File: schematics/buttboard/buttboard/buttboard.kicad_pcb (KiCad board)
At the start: 4 copper layers, 84 x 65 mm, 11 parts, among them J1 Conn_01x05

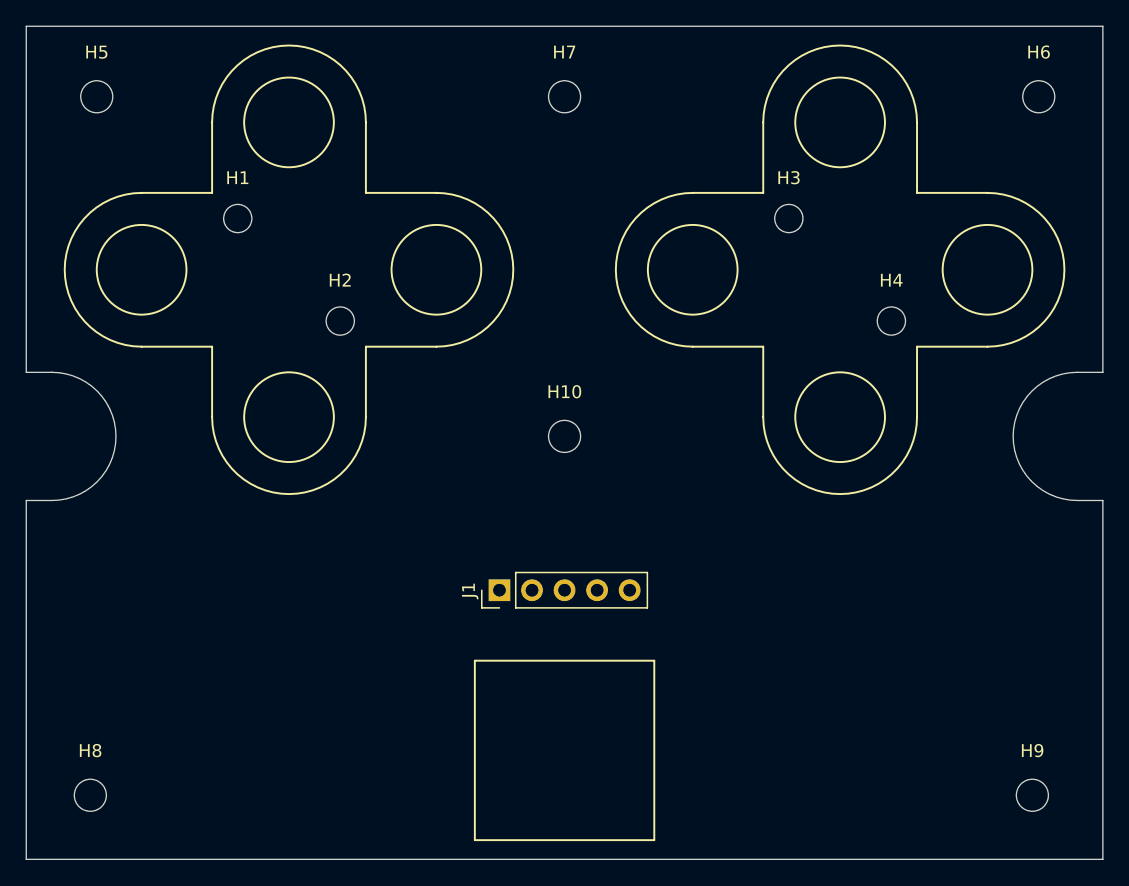
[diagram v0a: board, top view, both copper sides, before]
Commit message: Mounting points for mainboard added. Adjusted position of track ball on buttboard.
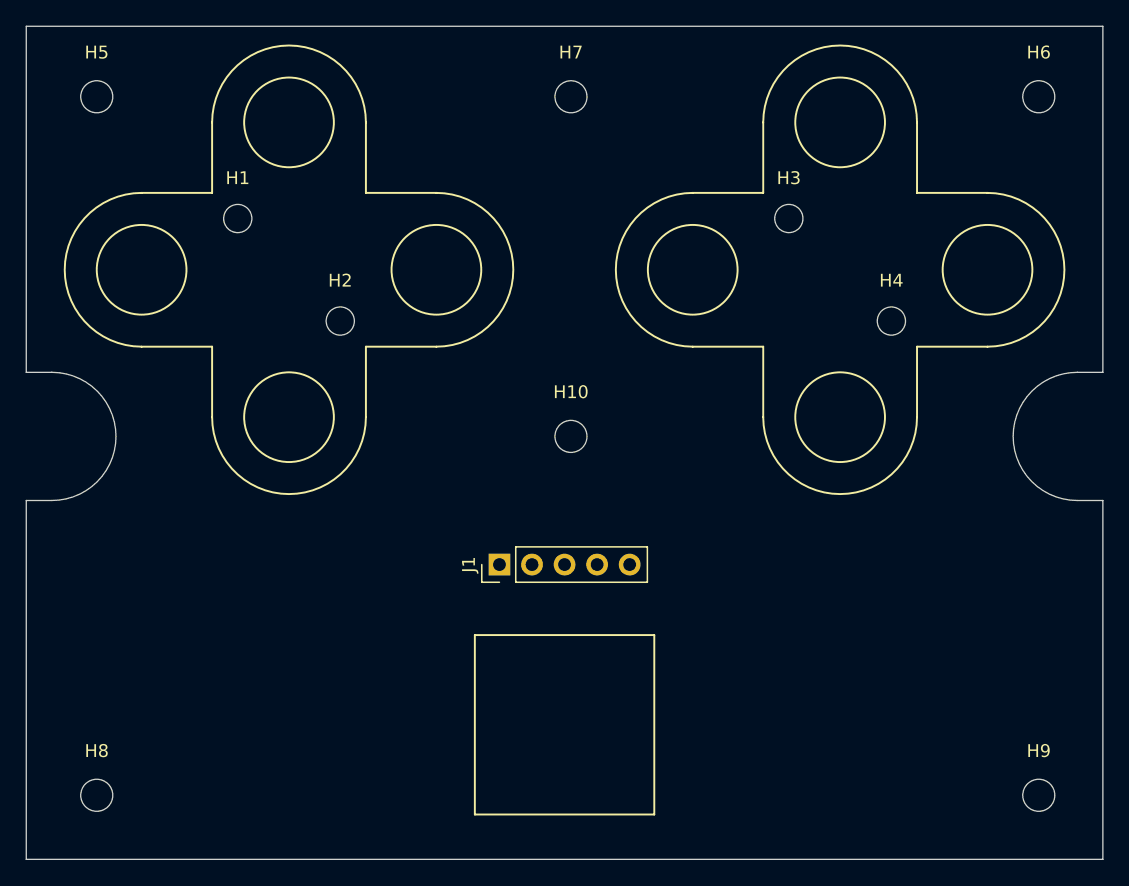
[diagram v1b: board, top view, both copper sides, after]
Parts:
- moved J1 2.00 mm to (147.4, 99.0)
- moved H10 0.50 mm to (153.0, 89.0)
- moved H7 0.50 mm to (153.0, 62.5)
- moved H8 0.50 mm to (116.0, 117.0)
- moved H9 0.50 mm to (189.5, 117.0)
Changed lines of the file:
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@@
 	(footprint "Connector_PinHeader_2.54mm:PinHeader_1x05_P2.54mm_Vertical"
 		(layer "F.Cu")
-		(at 147.42 101 90)
+		(at 147.42 99 90)
 		(descr "Through hole straight pin header, 1x05, 2.54mm pitch, single row")
 		(tags "Through hole pin header THT 1x05 2.54mm single row")
@@
 	(footprint "MountingHole:MountingHole_2.5mm"
 		(layer "F.Cu")
-		(at 115.5 117)
+		(at 116 117)
 		(descr "Mounting Hole 2.5mm, no annular, generated by kicad-footprint-generator mountinghole.py")
 		(tags "mountinghole")
@@
 	(footprint "MountingHole:MountingHole_2.5mm"
 		(layer "F.Cu")
-		(at 189 117)
+		(at 189.5 117)
 		(descr "Mounting Hole 2.5mm, no annular, generated by kicad-footprint-generator mountinghole.py")
 		(tags "mountinghole")
@@
 	(footprint "MountingHole:MountingHole_2.5mm"
 		(layer "F.Cu")
-		(at 152.5 62.5)
+		(at 153 62.5)
 		(descr "Mounting Hole 2.5mm, no annular, generated by kicad-footprint-generator mountinghole.py")
 		(tags "mountinghole")
@@
 	(footprint "MountingHole:MountingHole_2.5mm"
 		(layer "F.Cu")
-		(at 152.5 89)
+		(at 153 89)
 		(descr "Mounting Hole 2.5mm, no annular, generated by kicad-footprint-generator mountinghole.py")
 		(tags "mountinghole")
@@
 	)
 	(gr_rect
-		(start 145.5 106.5)
-		(end 159.5 120.5)
+		(start 145.5 104.5)
+		(end 159.5 118.5)
 		(stroke
 			(width 0.15)
@@
 	)
 	(gr_line
-		(start 152.5 129.5)
-		(end 152.5 46.5)
+		(start 153 129.5)
+		(end 153 46.5)
 		(stroke
 			(width 0.15)
@@
 		(layer "F.SilkS")
 		(pts
-			(xy 116 62.5) (xy 152.5 62.5)
+			(xy 116 117) (xy 110.5 118.5)
+		)
+		(height 8)
+		(orientation 0)
+		(format
+			(prefix "")
+			(suffix "")
+			(units 3)
+			(units_format 0)
+			(precision 4)
+			(suppress_zeroes yes)
+		)
+		(style
+			(thickness 0.15)
+			(arrow_length 1.27)
+			(text_position_mode 0)
+			(arrow_direction outward)
+			(extension_height 0.58642)
+			(extension_offset 0.5)
+			(keep_text_aligned yes)
+		)
+		(gr_text "5,5"
+			(at 113.25 123.85 0)
+			(layer "F.SilkS")
+			(effects
+				(font
+					(size 1 1)
+					(thickness 0.15)
+				)
+			)
+		)
+	)
+	(dimension
+		(type orthogonal)
+		(layer "F.SilkS")
+		(pts
+			(xy 159.5 111.5) (xy 194.5 111.5)
+		)
+		(height -2)
+		(orientation 0)
+		(format
+			(prefix "")
+			(suffix "")
+			(units 3)
+			(units_format 0)
+			(precision 4)
+			(suppress_zeroes yes)
+		)
+		(style
+			(thickness 0.15)
+			(arrow_length 1.27)
+			(text_position_mode 0)
+			(arrow_direction outward)
+			(extension_height 0.58642)
+			(extension_offset 0.5)
+			(keep_text_aligned yes)
+		)
+		(gr_text "35"
+			(at 177 108.35 0)
+			(layer "F.SilkS")
+			(effects
+				(font
+					(size 1 1)
+					(thickness 0.15)
+				)
+			)
+		)
+	)
+	(dimension
+		(type orthogonal)
+		(layer "F.SilkS")
+		(pts
+			(xy 116 62.5) (xy 110.5 61.5)
+		)
+		(height -8.5)
+		(orientation 0)
+		(format
+			(prefix "")
+			(suffix "")
+			(units 3)
+			(units_format 0)
+			(precision 4)
+			(suppress_zeroes yes)
+		)
+		(style
+			(thickness 0.15)
+			(arrow_length 1.27)
+			(text_position_mode 0)
+			(arrow_direction outward)
+			(extension_height 0.58642)
+			(extension_offset 0.5)
+			(keep_text_aligned yes)
+		)
+		(gr_text "5,5"
+			(at 113.25 52.85 0)
+			(layer "F.SilkS")
+			(effects
+				(font
+					(size 1 1)
+					(thickness 0.15)
+				)
+			)
+		)
+	)
+	(dimension
+		(type orthogonal)
+		(layer "F.SilkS")
+		(pts
+			(xy 116.5 62.5) (xy 153 62.5)
 		)
 		(height -21)
@@
 		)
 		(gr_text "36,5"
-			(at 134.25 40.35 0)
+			(at 134.75 40.35 0)
 			(layer "F.SilkS")
 			(effects
@@
 		(layer "F.SilkS")
 		(pts
+			(xy 145.5 108) (xy 110.5 107.5)
+		)
+		(height 2.5)
+		(orientation 0)
+		(format
+			(prefix "")
+			(suffix "")
+			(units 3)
+			(units_format 0)
+			(precision 4)
+			(suppress_zeroes yes)
+		)
+		(style
+			(thickness 0.15)
+			(arrow_length 1.27)
+			(text_position_mode 0)
+			(arrow_direction outward)
+			(extension_height 0.58642)
+			(extension_offset 0.5)
+			(keep_text_aligned yes)
+		)
+		(gr_text "35"
+			(at 128 109.35 0)
+			(layer "F.SilkS")
+			(effects
+				(font
+					(size 1 1)
+					(thickness 0.15)
+				)
+			)
+		)
+	)
+	(dimension
+		(type orthogonal)
+		(layer "F.SilkS")
+		(pts
 			(xy 116 62.5) (xy 115.5 117)
 		)
@@
 		(layer "F.SilkS")
 		(pts
-			(xy 152.5 62.5) (xy 189.5 62.5)
+			(xy 153 62.5) (xy 189.5 62.5)
 		)
 		(height -21)
@@
 			(keep_text_aligned yes)
 		)
-		(gr_text "37"
-			(at 171 40.35 0)
+		(gr_text "36,5"
+			(at 171.25 40.35 0)
 			(layer "F.SilkS")
 			(effects
@@
 		(layer "F.SilkS")
 		(pts
-			(xy 115.5 117) (xy 189 117)
+			(xy 116 117) (xy 189.5 117)
 		)
 		(height 9.5)
@@
 		)
 		(gr_text "73,5"
-			(at 152.25 125.35 0)
+			(at 152.75 125.35 0)
 			(layer "F.SilkS")
 			(effects
@@
 			(effects
 				(font
-					(size 1 1)
-					(thickness 0.15)
-				)
-			)
-		)
-	)
-	(dimension
-		(type orthogonal)
-		(layer "Edge.Cuts")
-		(pts
-			(xy 152.5 94) (xy 117.5 94)
-		)
-		(height 18)
-		(orientation 0)
-		(format
-			(prefix "")
-			(suffix "")
-			(units 3)
-			(units_format 0)
-			(precision 4)
-			(suppress_zeroes yes)
-		)
-		(style
-			(thickness 0.1)
-			(arrow_length 1.27)
-			(text_position_mode 0)
-			(arrow_direction outward)
-			(extension_height 0.58642)
-			(extension_offset 0.5)
-			(keep_text_aligned yes)
-		)
-		(gr_text "35"
-			(at 135 110.85 0)
-			(layer "Edge.Cuts")
-			(effects
-				(font
-					(size 1 1)
-					(thickness 0.15)
-				)
-			)
-		)
-	)
-	(dimension
-		(type orthogonal)
-		(layer "Edge.Cuts")
-		(pts
-			(xy 152.5 94) (xy 187.5 94)
-		)
-		(height 17)
-		(orientation 0)
-		(format
-			(prefix "")
-			(suffix "")
-			(units 3)
-			(units_format 0)
-			(precision 4)
-			(suppress_zeroes yes)
-		)
-		(style
-			(thickness 0.1)
-			(arrow_length 1.27)
-			(text_position_mode 0)
-			(arrow_direction outward)
-			(extension_height 0.58642)
-			(extension_offset 0.5)
-			(keep_text_aligned yes)
-		)
-		(gr_text "35"
-			(at 170 109.85 0)
-			(layer "Edge.Cuts")
-			(effects
-				(font

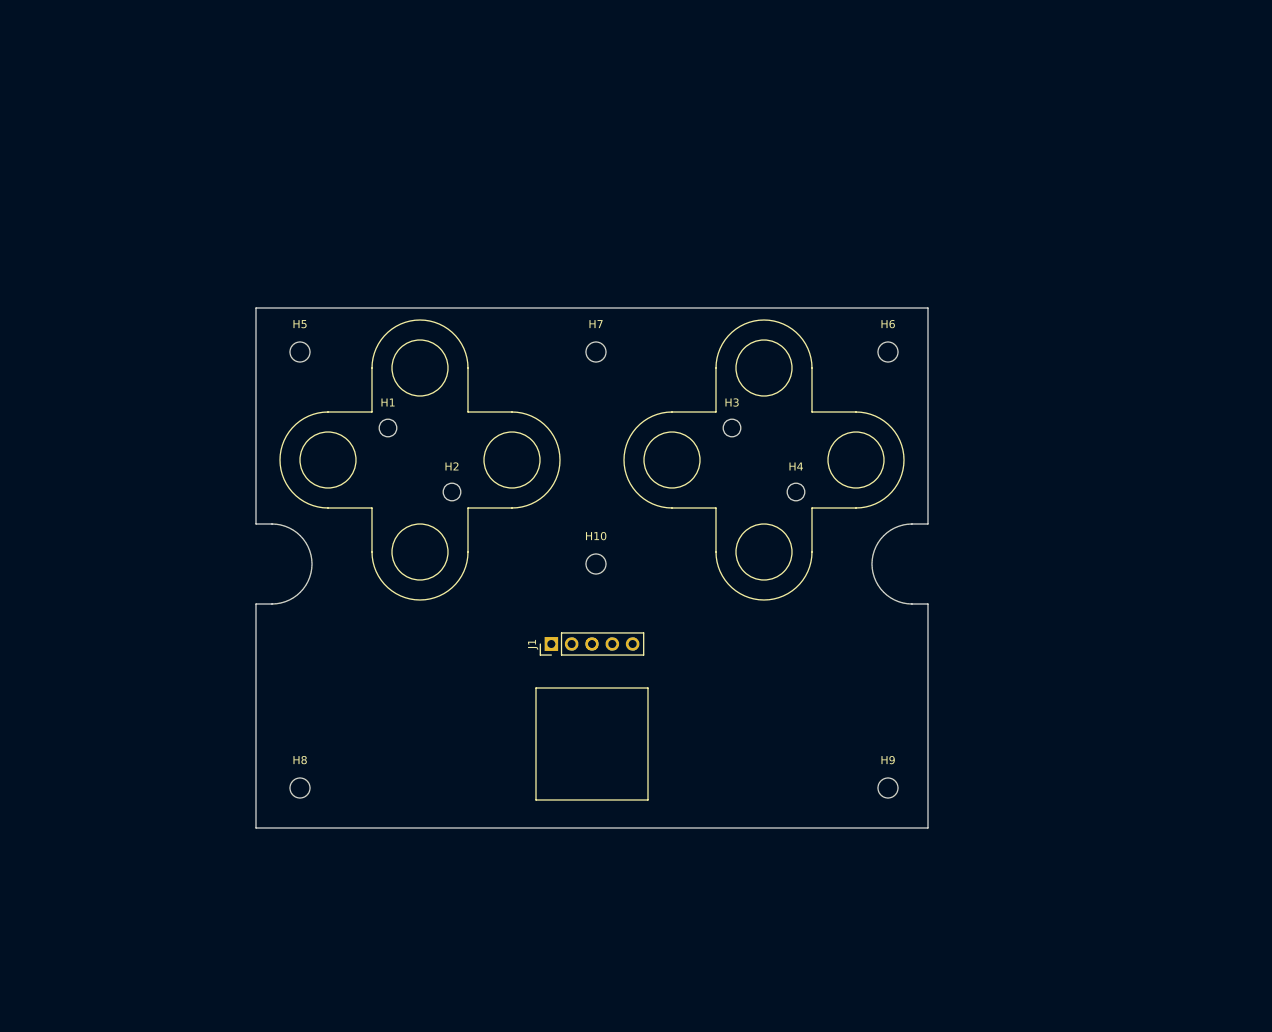
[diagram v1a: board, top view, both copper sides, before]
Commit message: Added membrane button footprint to buttboard.
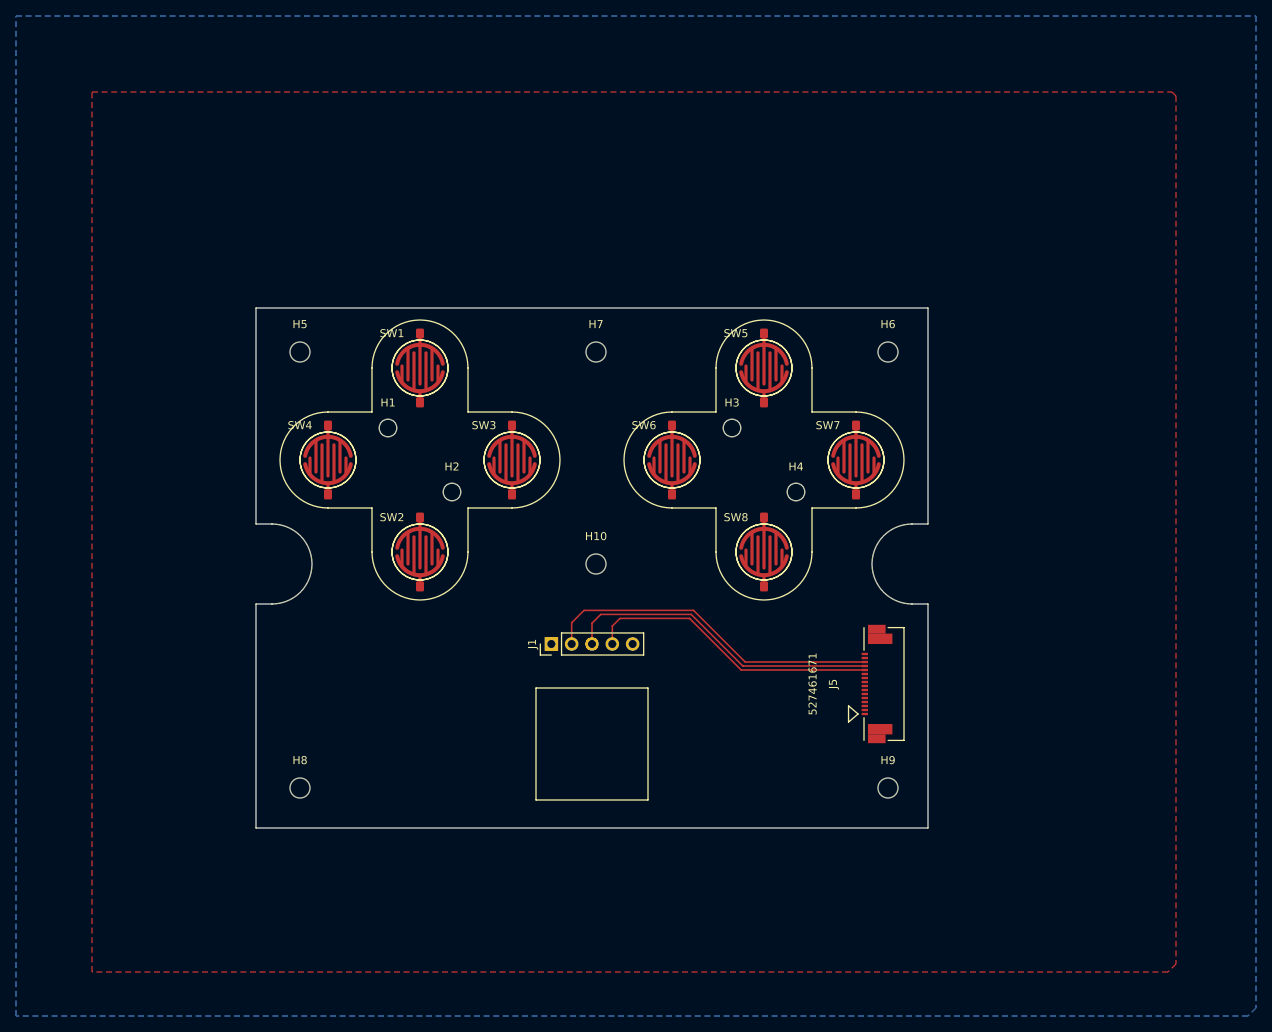
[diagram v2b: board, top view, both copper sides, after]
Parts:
- added J5: 527461671, CON_527461671_MOL:CON_527461671_MOL, F.Cu at (189.0, 104.0)
- added SW1: N, MEMBRANE:MEMBRANE_A, F.Cu at (131.0, 64.5)
- added SW2: S, MEMBRANE:MEMBRANE_A, F.Cu at (131.0, 87.5)
- added SW3: E, MEMBRANE:MEMBRANE_A, F.Cu at (142.5, 76.0)
- added SW4: W, MEMBRANE:MEMBRANE_A, F.Cu at (119.5, 76.0)
- added SW5: A, MEMBRANE:MEMBRANE_A, F.Cu at (174.0, 64.5)
- added SW6: B, MEMBRANE:MEMBRANE_A, F.Cu at (162.5, 76.0)
- added SW7: C, MEMBRANE:MEMBRANE_A, F.Cu at (185.5, 76.0)
- added SW8: D, MEMBRANE:MEMBRANE_A, F.Cu at (174.0, 87.5)
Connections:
- J1 pad 2: TB_INT -> TRACKBALL_INTERRUPT
- J1 pad 3: TB_SCL -> I2C_SCL
- J1 pad 4: TB_SDA -> I2C_SDA
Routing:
- net TRACKBALL_INTERRUPT: track 0.00 -> 42.6 mm
- net I2C_SCL: track 0.00 -> 39.8 mm
- net I2C_SDA: track 0.00 -> 36.9 mm
- added copper zone on B.Cu, net GND
- added copper zone on F.Cu, net GND
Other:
- copper layers 4 -> 2

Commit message: Replaced membrane buttons with tactile buttons on buttboard.
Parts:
- SW1, SW2, SW3, SW4, SW5, SW6, SW7, SW8: footprint MEMBRANE:MEMBRANE_A -> Button_Switch_THT:SW_PUSH_6mm_H7.3mm
- moved SW1 3.95 mm to (127.8, 62.2)
- moved SW2 3.95 mm to (127.8, 85.2)
- moved SW3 3.95 mm to (139.2, 73.8)
- moved SW4 3.95 mm to (116.2, 73.8)
- moved SW5 3.95 mm to (170.8, 62.2)
- moved SW6 3.95 mm to (159.2, 73.8)
- moved SW7 3.95 mm to (182.2, 73.8)
- moved SW8 3.95 mm to (170.8, 85.2)
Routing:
- net BTN_A: track 0.00 -> 56.0 mm, vias 0 -> 1
- net BTN_B: track 0.00 -> 47.4 mm, vias 0 -> 1
- net BTN_C: track 0.00 -> 44.7 mm, vias 0 -> 1
- net BTN_D: track 0.00 -> 30.4 mm, vias 0 -> 1
- net 3V3: track 0.00 -> 29.7 mm, vias 0 -> 1

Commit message: More work on buttboard.
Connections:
- J5 pad 6: unconnected-(J5-Pad6) -> BTN_DPAD_N
- J5 pad 7: unconnected-(J5-Pad7) -> BTN_DPAD_S
- J5 pad 8: unconnected-(J5-Pad8) -> BTN_DPAD_E
- J5 pad 9: unconnected-(J5-Pad9) -> BTN_DPAD_W
- SW1 pad 1: unconnected-(SW1-Pad1) -> BTN_DPAD_N
- SW2 pad 1: unconnected-(SW2-Pad1) -> BTN_DPAD_S
- SW3 pad 1: unconnected-(SW3-Pad1) -> BTN_DPAD_E
- SW4 pad 1: unconnected-(SW4-Pad1) -> BTN_DPAD_W
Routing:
- net BTN_DPAD_N: track 0.00 -> 118.5 mm, vias 0 -> 1
- net BTN_DPAD_W: track 0.00 -> 101.2 mm
- net BTN_DPAD_E: track 0.00 -> 86.2 mm, vias 0 -> 1
- net BTN_DPAD_S: track 0.00 -> 84.2 mm, vias 0 -> 1
- net BTN_A: track 56.0 -> 64.8 mm
- net BTN_D: track 30.4 -> 39.1 mm
- net BTN_B: track 47.4 -> 55.6 mm
- net BTN_C: track 44.7 -> 52.6 mm
- net I2C_SDA: track 36.9 -> 32.9 mm
- net GND: track 0.00 -> 3.94 mm, vias 0 -> 31
- net I2C_SCL: track 39.8 -> 38.2 mm
- net TRACKBALL_INTERRUPT: track 42.6 -> 41.1 mm
